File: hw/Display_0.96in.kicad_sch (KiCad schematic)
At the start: 3 parts, among them J5 BM20B(0.8)-10DS-0.4V

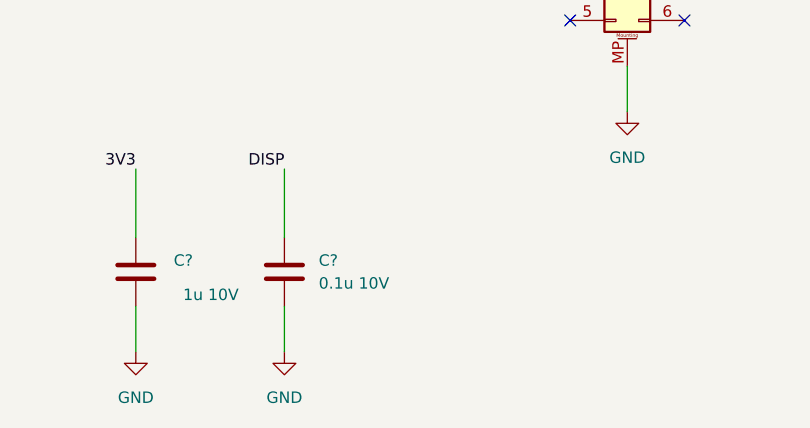
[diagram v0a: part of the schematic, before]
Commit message: updated 100nF model
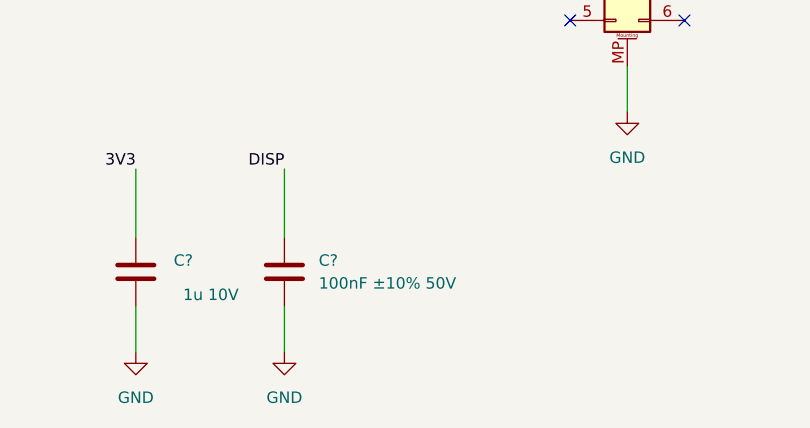
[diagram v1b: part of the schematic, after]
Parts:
- C?: value 0.1u 10V -> 100nF ±10% 50V; LCSC C1853551 -> C49678; Vendor Model CC0805JKX7R0BB104 -> CC0805KRX7R9BB104
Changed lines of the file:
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@@
       (effects (font (size 1.27 1.27)) (justify left))
     )
-    (property "Value" "0.1u 10V" (at 104.14 97.79 0)
+    (property "Value" "100nF ±10% 50V" (at 104.14 97.79 0)
       (effects (font (size 1.27 1.27)) (justify left))
     )
@@
       (effects (font (size 1.27 1.27)) hide)
     )
-    (property "LCSC" "C1853551" (at 100.33 96.52 0)
+    (property "LCSC" "C49678" (at 100.33 96.52 0)
       (effects (font (size 1.27 1.27)) hide)
     )
@@
       (effects (font (size 1.27 1.27)) hide)
     )
-    (property "Vendor Model" "CC0805JKX7R0BB104" (at 100.33 96.52 0)
+    (property "Vendor Model" "CC0805KRX7R9BB104" (at 100.33 96.52 0)
       (effects (font (size 1.27 1.27)) hide)
     )

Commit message: updated sheets information
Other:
- company: (none) -> Qingdao IotPi Information Technology Ltd.,
- title: (none) -> KiCad 2023 Shen Zhen Badge
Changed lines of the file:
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@@
 (kicad_sch (version 20230121) (generator eeschema)
   (paper "A4")
+  (title_block
+    (title "KiCad 2023 Shen Zhen Badge")
+    (date "2023-09-04")
+    (rev "1")
+    (company "Qingdao IotPi Information Technology Ltd.,")
+    (comment 1 "Designed by Yang Hongbo")
+  )
   (no_connect (at 144.78 63.5))
   (no_connect (at 144.78 68.58))
